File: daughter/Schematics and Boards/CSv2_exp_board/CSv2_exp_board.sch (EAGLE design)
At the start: 103 parts, among them J1 HIROSE-DF40_44-PIN_CONNECTORS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, J3 CORTEX_DEBUG_SMD, J301 HIROSE-DF40_44-PIN_CONNECTORS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, J7 J-USB-HIROSE-MICRO-USB, U1 LOADSWITCH-MIC94164, U10 LOADSWITCH-MIC94164, U11 BMI160, U2 ADA4841-1YRJZ-R7, U205 MPL3115A2, U3 Value, U4 RFM69HCW, U5 Value, U6 Value, U7 LOADSWITCH-MIC94164, U8 LOADSWITCH-MIC94164, U9 LOADSWITCH-MIC94164, X1 32.768kHz, X2 32.768, X4 uFL

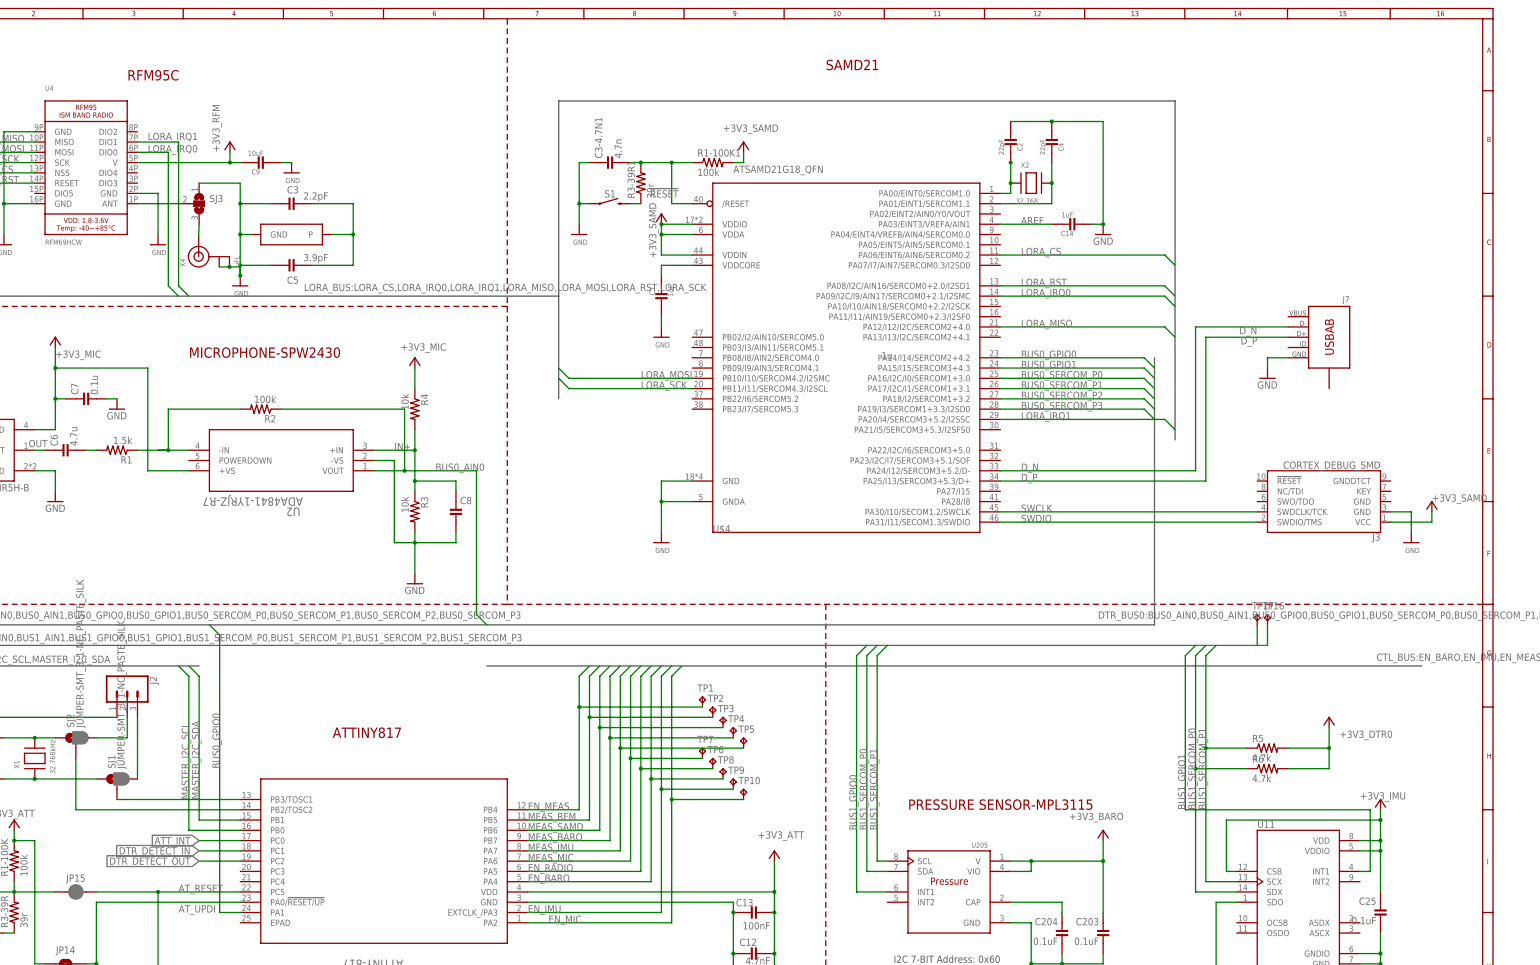
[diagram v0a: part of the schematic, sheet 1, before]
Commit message: DTR-reorganized eagle folder
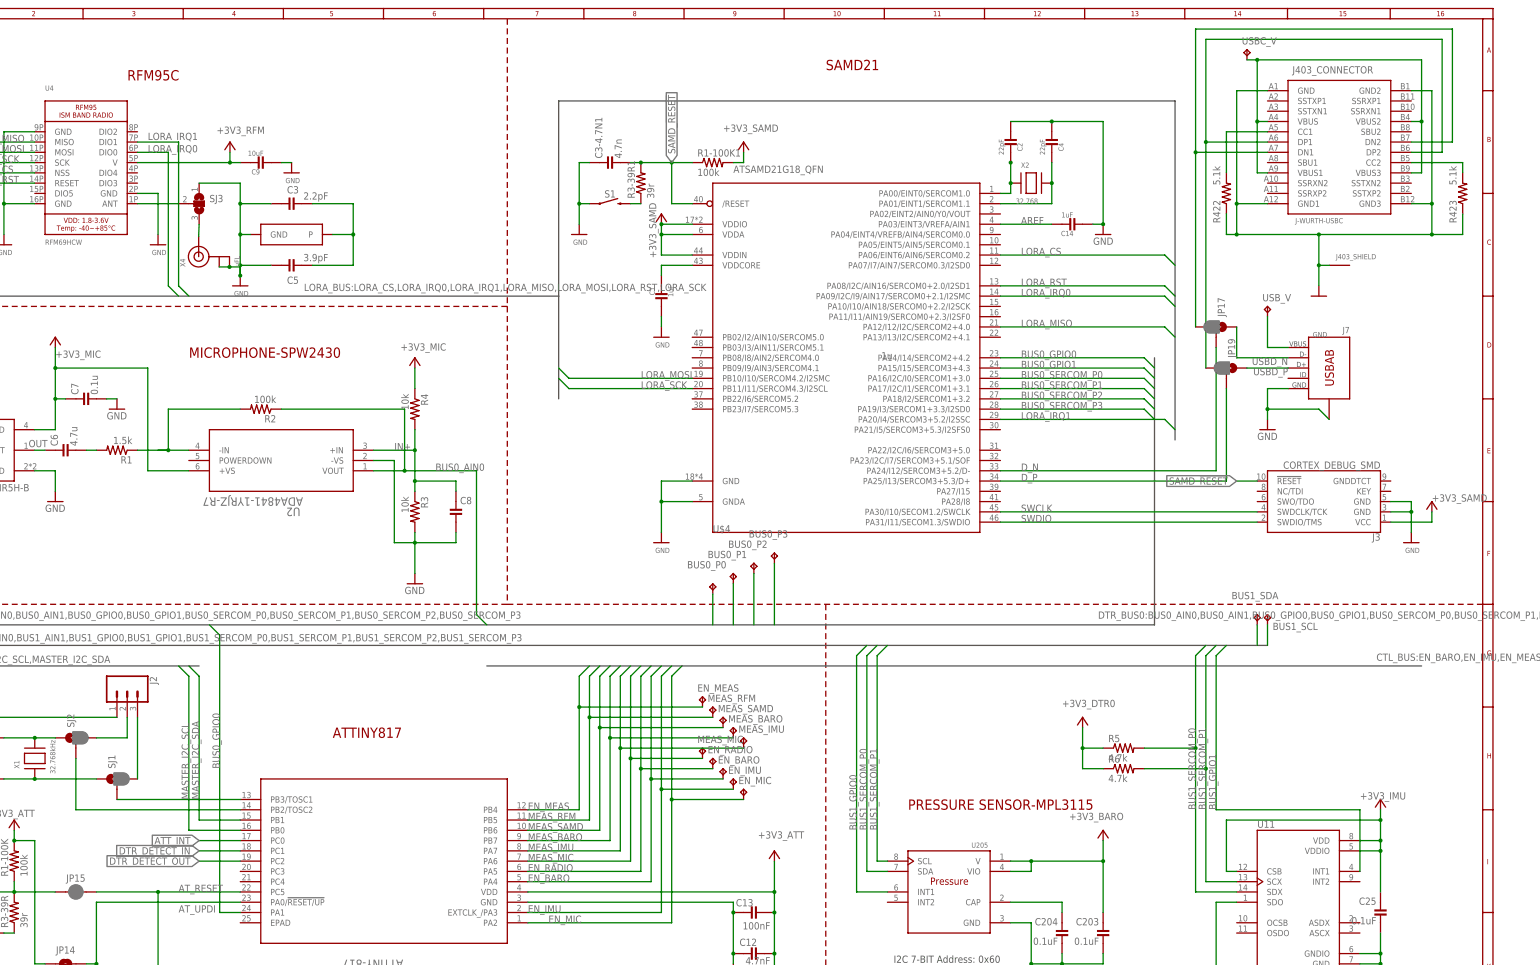
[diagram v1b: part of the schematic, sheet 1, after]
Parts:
- added BUS0_P0, BUS0_P1, BUS0_P2, BUS0_P3, USBC_V, USB_V: TPTP14SQ, TestPoints:TPTP14SQ
- added J403: J-WURTH-USBC, Connectors:J-WURTH-USBC
- added JP17, JP19: JUMPER-SMT_3_1-NC_PASTE_NO-SILK, Connectors:JUMPER-SMT_3_1-NC_PASTE_NO-SILK
- added R422, R423: 5.1k, Resistors:R-0603
- renumbered TP1 to EN_MEAS, TP10 to EN_MIC, TP11 to DTR_DETECT_IN, TP12 to ATT_INT, TP13 to DTR_DETECT_OUT, TP14 to ATT_SCL, TP15 to ATT_SDA, TP16 to BUS1_SCL, TP17 to BUS1_SDA, TP2 to MEAS_RFM, TP3 to MEAS_SAMD, TP4 to MEAS_BARO, TP5 to MEAS_IMU, TP6 to EN_RADIO, TP7 to MEAS_MIC, TP8 to EN_BARO, TP9 to EN_IMU
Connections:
- removed net N$9: C3-4.7N1.2, R1-100K1.1, R3-39R1.2, U$4./RESET
- new net CC1: J403_CONNECTOR.CC1, R422.2
- new net CC2: J403_CONNECTOR.CC2, R423.2
- new net N$17: J7.VBUS, USB_V.TP
- new net SAMD_!RESET: C3-4.7N1.2, J3.!RESET, R1-100K1.1, R3-39R1.2, U$4./RESET
- new net USBCD_N: J403_CONNECTOR.DN1, J403_CONNECTOR.DN2, JP17.3
- new net USBCD_P: J403_CONNECTOR.DP1, J403_CONNECTOR.DP2, JP19.3
- new net USBD_N: J7.D-, JP17.1
- new net USBD_P: J7.D+, JP19.1
- new net VBUS: J403_CONNECTOR.VBUS, J403_CONNECTOR.VBUS1, J403_CONNECTOR.VBUS2, J403_CONNECTOR.VBUS3, USBC_V.TP
- net +3V3_DTR0: now also R5.1, R6.1; no longer R5.2, R6.2
- net BUS0_SERCOM_P0: now also BUS0_P0.TP
- net BUS0_SERCOM_P1: now also BUS0_P1.TP
- net BUS0_SERCOM_P2: now also BUS0_P2.TP
- net BUS0_SERCOM_P3: now also BUS0_P3.TP
- net BUS1_SERCOM_P0: now also R5.2; no longer R6.1
- net BUS1_SERCOM_P1: now also R6.2; no longer R5.1
- net D_N: now also JP17.2; no longer J7.D-
- net D_P: now also JP19.2; no longer J7.D+
- net GND: now also J3.GND@5, J403_CONNECTOR.GND, J403_CONNECTOR.GND1, J403_CONNECTOR.GND2, J403_CONNECTOR.GND3, J403_SHIELD.SHIELD, J7.SHIELD, R422.1, R423.1
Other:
- moved on the sheet: J7, R5, R6

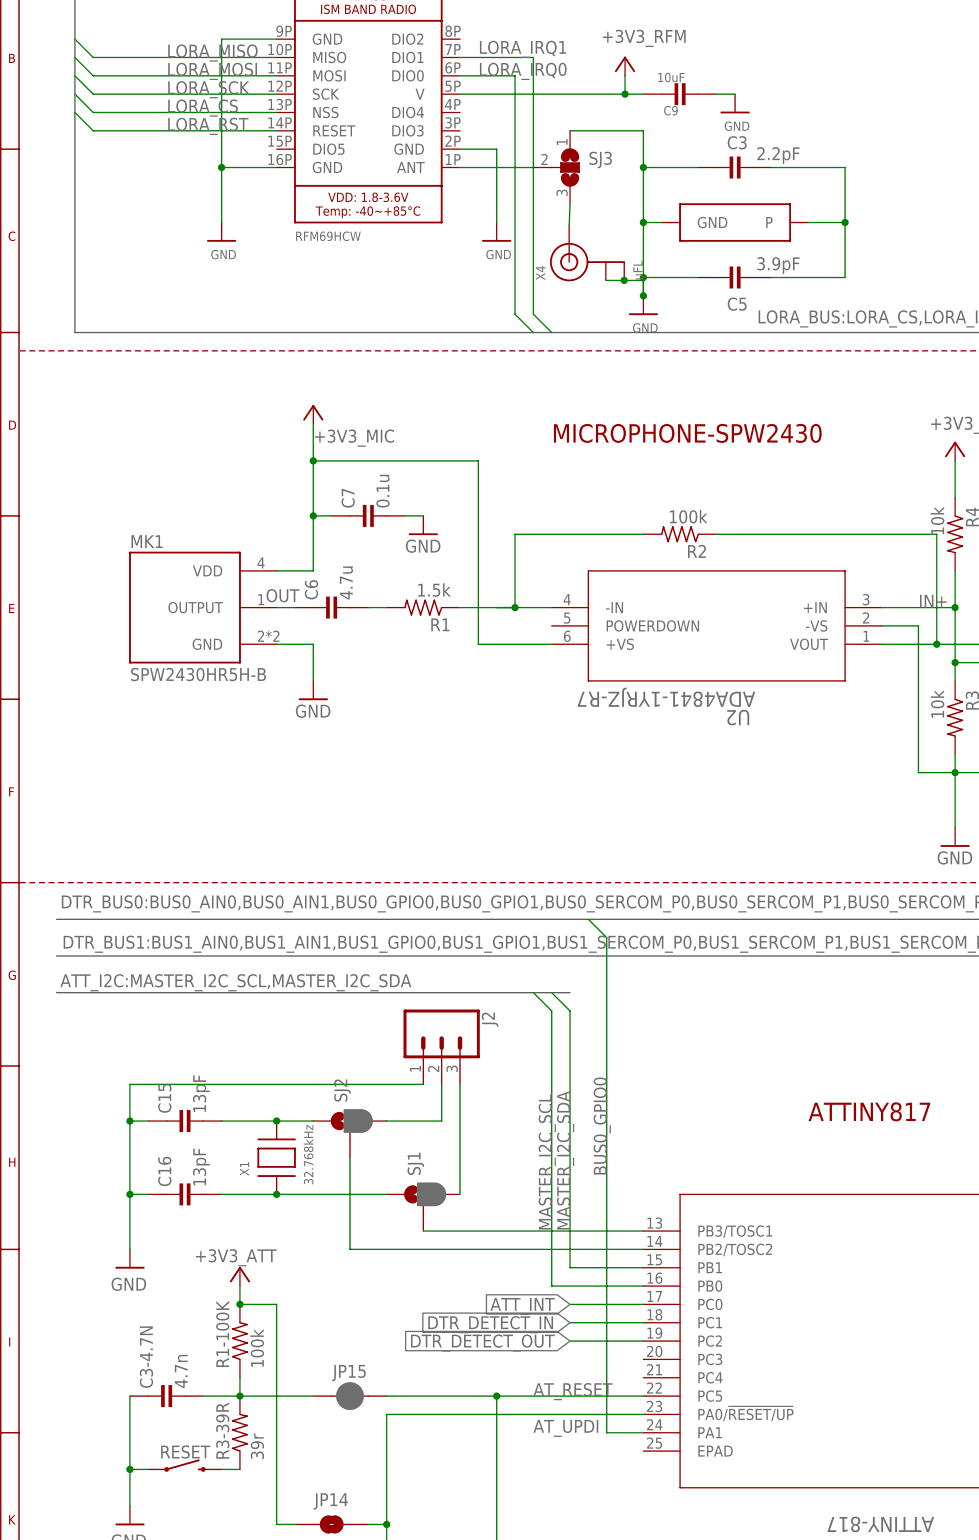
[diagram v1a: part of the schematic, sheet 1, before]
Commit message: DTR-placement + half manual routing
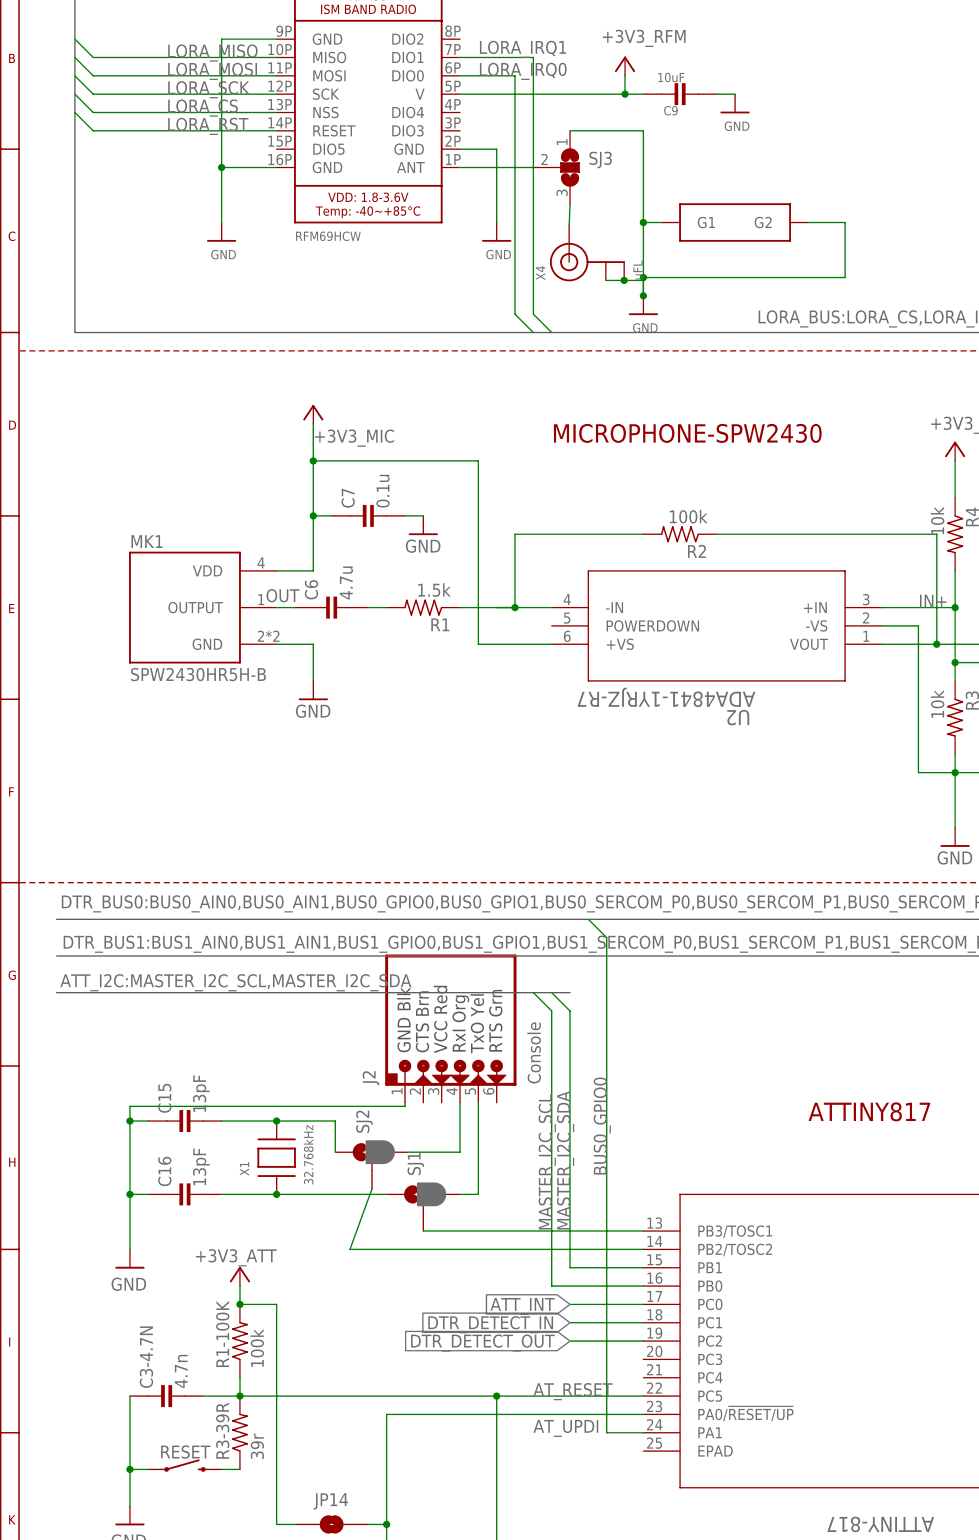
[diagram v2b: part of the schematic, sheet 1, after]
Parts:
- removed C3: 2.2pF, Capacitors:C-0402
- removed C5: 3.9pF, Capacitors:C-0402
- removed JP15: JUMPER-SMT_2_NC_PASTE, Connectors:JUMPER-SMT_2_NC_PASTE
- ATT_INT, ATT_SCL, ATT_SDA, BUS0_P0, BUS0_P1, BUS0_P2, BUS0_P3, BUS1_SCL, BUS1_SDA, DTR_DETECT_IN, DTR_DETECT_OUT, EN_BARO, EN_IMU, EN_MEAS, EN_MIC, EN_RADIO, MEAS_BARO, MEAS_IMU, MEAS_MIC, MEAS_RFM, MEAS_SAMD, USBC_V, USB_V: value TPTP14SQ -> TPTP10SQ; device TestPoints:TPTP14SQ -> TestPoints:TPTP10SQ
- J2: value (none) -> J-SERIAL-PORT; device Connectors:J-SCR-3SL -> Connectors:J-SERIAL-PORT
- J301: value HIROSE-DF40_44-PIN_CONNECTORS-RECEPTACLE -> HIROSE-DF40_44-PIN_CONNECTORS-HEADER; device Connectors:HIROSE-DF40_44-PIN_CONNECTORS-RECEPTACLE -> Connectors:HIROSE-DF40_44-PIN_CONNECTORS-HEADER
- JP1, JP10, JP11, JP12, JP13, JP2, JP3, JP4, JP5, JP6, JP7, JP8, JP9: value JUMPER-SMT_2_NC_PASTE -> JUMPER-SMT_2_NC_PASTELG_NO-SILK; device Connectors:JUMPER-SMT_2_NC_PASTE -> Connectors:JUMPER-SMT_2_NC_PASTELG_NO-SILK
- R5, R6: device Resistors:R-0805 -> Resistors:R-0603
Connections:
- net 3V_LD_SW renamed +3V3_SAMD_IN
- net 3V_LD_SW1 renamed +3V3_RFM_IN
- net 3V_LD_SW2 renamed +3V3_BARO_IN
- net 3V_LD_SW3 renamed +3V3_IMU_IN
- net 3V_LD_SW4 renamed +3V3_MIC_IN
- net N$11 renamed +3V3_IMU_PWR
- net N$13 renamed +3V3_BARO_PWR
- net N$14 renamed +3V3_RFM_PWR
- net N$15 renamed +3V3_SAMD_PWR
- net N$16 renamed +3V3_NMEAS
- net N$3 renamed +3V3_MIC_PWR
- net N$4 renamed +3V3_MEAS
- net N0 renamed +3V3_SAMD_OUT
- net N1 renamed +3V3_RFM_OUT
- net N2 renamed +3V3_BARO_OUT
- net N3 renamed +3V3_IMU_OUT
- net N4 renamed +3V3_MIC_OUT
- removed net +3V3: JP12.1, R_SENSE.1
- removed net N$21: J2.3, SJ1.3
- removed net N$24: C3-4.7N.2, JP15.1, R1-100K.1, R3-39R.2
- removed net N$25: C3.2, C5.2, U$1.P
- new net N$3: J2.TX-O, SJ1.3
- net +3V3_DTR: now also JP12.1, R_SENSE.1
- net AT_RESET: now also C3-4.7N.2, R1-100K.1, R3-39R.2; no longer JP15.2
- net GND: now also J2.GND, U$1.G1, U$1.G2; no longer C3.1, C5.1, J2.1, U$1.GND
- net N$20: now also J2.RX-I; no longer J2.2
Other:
- moved on the sheet: SJ2

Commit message: DTR-replacement and manual routing
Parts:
- removed C3-4.7N1: 4.7n, Capacitors:C-0603
- removed J403: J-WURTH-USBC, Connectors:J-WURTH-USBC
- removed JP17, JP19: JUMPER-SMT_3_1-NC_PASTE_NO-SILK, Connectors:JUMPER-SMT_3_1-NC_PASTE_NO-SILK
- removed R1-100K1: 100k, Resistors:R-0603
- removed R3-39R1: 39r, Resistors:R-0603
- removed R422, R423: 5.1k, Resistors:R-0603
- removed RESET, S1: MOMENTARY-SWITCH-SPST-SMD-5.2MM, Switches:MOMENTARY-SWITCH-SPST-SMD-5.2MM
- removed U$1: ILA09_CHIP_ANTENNASMD, CommonSense-DTR-v1:ILA09_CHIP_ANTENNASMD
- removed USBC_V: TPTP10SQ, TestPoints:TPTP10SQ
- added A1: ILA09_CHIP_ANTENNA, CommonSense-DTR-v1:ILA09_CHIP_ANTENNA
- added C3: 3.9p, CommonSense-DTR-v1:C0402-ANT0402
- added C5: 2.2p, CommonSense-DTR-v1:C0402-ANT0402
- added SW1, SW2: SPST_TACT-KMR2, adafruit:SPST_TACT-KMR2
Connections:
- removed net !RESET: R3-39R1.1, S1.2
- removed net CC1: J403_CONNECTOR.CC1, R422.2
- removed net CC2: J403_CONNECTOR.CC2, R423.2
- removed net USBCD_N: J403_CONNECTOR.DN1, J403_CONNECTOR.DN2, JP17.3
- removed net USBCD_P: J403_CONNECTOR.DP1, J403_CONNECTOR.DP2, JP19.3
- removed net USBD_N: J7.D-, JP17.1
- removed net USBD_P: J7.D+, JP19.1
- removed net VBUS: J403_CONNECTOR.VBUS, J403_CONNECTOR.VBUS1, J403_CONNECTOR.VBUS2, J403_CONNECTOR.VBUS3, USBC_V.TP
- new net N$4: A1.G2, C3.2, C5.2
- net +3V3_SAMD: no longer R1-100K1.2
- net D_N: now also J7.D-; no longer JP17.2
- net D_P: now also J7.D+; no longer JP19.2
- net GND: now also A1.G1, C3.1, C5.1, SW1.P, SW1.P1, SW2.P, SW2.P1; no longer C3-4.7N1.1, J403_CONNECTOR.GND, J403_CONNECTOR.GND1, J403_CONNECTOR.GND2, J403_CONNECTOR.GND3, J403_SHIELD.SHIELD, R422.1, R423.1, RESET.1, S1.1, U$1.G1, U$1.G2
- net N$12: now also SW1.S, SW1.S1; no longer RESET.2
- net SAMD_!RESET: now also SW2.S, SW2.S1; no longer C3-4.7N1.2, R1-100K1.1, R3-39R1.2

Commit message: DTR-hand-routing continued
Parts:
- removed EN_RADIO, MEAS_MIC, MEAS_RFM, MEAS_SAMD: TPTP10SQ, TestPoints:TPTP10SQ
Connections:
- net EN_RADIO: no longer EN_RADIO.TP
- net MEAS_MIC: no longer MEAS_MIC.TP
- net MEAS_RFM: no longer MEAS_RFM.TP
- net MEAS_SAMD: no longer MEAS_SAMD.TP
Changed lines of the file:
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@@
 <part name="+3V3_DTR1" library="Supplies" deviceset="+3V3" device=""/>
 <part name="EN_MEAS" library="TestPoints" deviceset="TP" device="TP10SQ" package3d_urn="urn:adsk.eagle:package:27962/1" value="TPTP10SQ"/>
-<part name="MEAS_RFM" library="TestPoints" deviceset="TP" device="TP10SQ" package3d_urn="urn:adsk.eagle:package:27962/1" value="TPTP10SQ"/>
-<part name="MEAS_SAMD" library="TestPoints" deviceset="TP" device="TP10SQ" package3d_urn="urn:adsk.eagle:package:27962/1" value="TPTP10SQ"/>
 <part name="MEAS_BARO" library="TestPoints" deviceset="TP" device="TP10SQ" package3d_urn="urn:adsk.eagle:package:27962/1" value="TPTP10SQ"/>
 <part name="MEAS_IMU" library="TestPoints" deviceset="TP" device="TP10SQ" package3d_urn="urn:adsk.eagle:package:27962/1" value="TPTP10SQ"/>
-<part name="EN_RADIO" library="TestPoints" deviceset="TP" device="TP10SQ" package3d_urn="urn:adsk.eagle:package:27962/1" value="TPTP10SQ"/>
-<part name="MEAS_MIC" library="TestPoints" deviceset="TP" device="TP10SQ" package3d_urn="urn:adsk.eagle:package:27962/1" value="TPTP10SQ"/>
 <part name="EN_BARO" library="TestPoints" deviceset="TP" device="TP10SQ" package3d_urn="urn:adsk.eagle:package:27962/1" value="TPTP10SQ"/>
 <part name="EN_IMU" library="TestPoints" deviceset="TP" device="TP10SQ" package3d_urn="urn:adsk.eagle:package:27962/1" value="TPTP10SQ"/>
@@
 <attribute name="TP_SIGNAL_NAME" x="204.47" y="102.87" size="1.778" layer="97"/>
 </instance>
-<instance part="MEAS_RFM" gate="G$1" x="205.74" y="101.6" smashed="yes">
-<attribute name="NAME" x="204.47" y="102.87" size="1.778" layer="95"/>
-<attribute name="TP_SIGNAL_NAME" x="207.01" y="100.33" size="1.778" layer="97"/>
-</instance>
-<instance part="MEAS_SAMD" gate="G$1" x="208.28" y="99.06" smashed="yes">
-<attribute name="NAME" x="207.01" y="100.33" size="1.778" layer="95"/>
-<attribute name="TP_SIGNAL_NAME" x="209.55" y="97.79" size="1.778" layer="97"/>
-</instance>
 <instance part="MEAS_BARO" gate="G$1" x="210.82" y="96.52" smashed="yes">
-<attribute name="NAME" x="209.55" y="97.79" size="1.778" layer="95"/>
 <attribute name="TP_SIGNAL_NAME" x="212.09" y="95.25" size="1.778" layer="97"/>
 </instance>
@@
 <attribute name="NAME" x="212.09" y="95.25" size="1.778" layer="95"/>
 <attribute name="TP_SIGNAL_NAME" x="214.63" y="92.71" size="1.778" layer="97"/>
-</instance>
-<instance part="EN_RADIO" gate="G$1" x="205.74" y="88.9" smashed="yes">
-<attribute name="NAME" x="204.47" y="90.17" size="1.778" layer="95"/>
-<attribute name="TP_SIGNAL_NAME" x="207.01" y="87.63" size="1.778" layer="97"/>
-</instance>
-<instance part="MEAS_MIC" gate="G$1" x="203.2" y="91.44" smashed="yes">
-<attribute name="NAME" x="201.93" y="92.71" size="1.778" layer="95"/>
-<attribute name="TP_SIGNAL_NAME" x="204.47" y="90.17" size="1.778" layer="97"/>
 </instance>
 <instance part="EN_BARO" gate="G$1" x="208.28" y="86.36" smashed="yes">
@@
 <wire x1="185.42" y1="88.9" x2="185.42" y2="109.22" width="0.1524" layer="91"/>
 <wire x1="185.42" y1="109.22" x2="187.96" y2="111.76" width="0.1524" layer="91"/>
-<pinref part="MEAS_MIC" gate="G$1" pin="TP"/>
 <wire x1="203.2" y1="88.9" x2="185.42" y2="88.9" width="0.1524" layer="91"/>
 <junction x="185.42" y="88.9"/>
@@
 <wire x1="177.8" y1="96.52" x2="177.8" y2="109.22" width="0.1524" layer="91"/>
 <wire x1="177.8" y1="109.22" x2="180.34" y2="111.76" width="0.1524" layer="91"/>
-<pinref part="MEAS_SAMD" gate="G$1" pin="TP"/>
 <wire x1="208.28" y1="96.52" x2="177.8" y2="96.52" width="0.1524" layer="91"/>
 <junction x="177.8" y="96.52"/>
@@
 <wire x1="175.26" y1="99.06" x2="175.26" y2="109.22" width="0.1524" layer="91"/>
 <wire x1="175.26" y1="109.22" x2="177.8" y2="111.76" width="0.1524" layer="91"/>
-<pinref part="MEAS_RFM" gate="G$1" pin="TP"/>
 <wire x1="205.74" y1="99.06" x2="175.26" y2="99.06" width="0.1524" layer="91"/>
 <junction x="175.26" y="99.06"/>
@@
 <wire x1="187.96" y1="86.36" x2="187.96" y2="109.22" width="0.1524" layer="91"/>
 <wire x1="187.96" y1="109.22" x2="190.5" y2="111.76" width="0.1524" layer="91"/>
-<pinref part="EN_RADIO" gate="G$1" pin="TP"/>
 <wire x1="205.74" y1="86.36" x2="187.96" y2="86.36" width="0.1524" layer="91"/>
 <junction x="187.96" y="86.36"/>
